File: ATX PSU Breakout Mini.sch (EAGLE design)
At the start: 39 parts, among them J1 ATX24RH, SW1 SW_PUSH_DPDT, T1 5V, T2 3V3, T3 12V, T4 GND, T5 ADJ, T6 -12V, U1 V_REG_317SINK, U2 TPS2513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

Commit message: Fixes and additions.
Thickened all traces, added resistors to the USB ports (you can use them
instead of the TPS2513)
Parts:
- added R10, R15: (no value), SparkFun-Resistors:RESISTOR0805-RES
- added R11, R16: 43K, SparkFun-Resistors:RESISTOR0805-RES
- added R12, R14, R17, R19: 51K, SparkFun-Resistors:RESISTOR0805-RES
- added R13, R18: 75K, SparkFun-Resistors:RESISTOR0805-RES
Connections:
- net 5V_STDBY: now also R16.1, R18.1
- net DM1: now also R15.1, R16.2, R17.1
- net DM2: now also R10.1, R11.2, R12.1
- net DP1: now also R15.2, R18.2, R19.1
- net DP2: now also R10.2, R13.2, R14.1
- net GND: now also R12.2, R14.2, R17.2, R19.2
- net USB_P4: now also R11.1, R13.1
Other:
- moved on the sheet: C3, R9, SJ1, U2, X1, X2

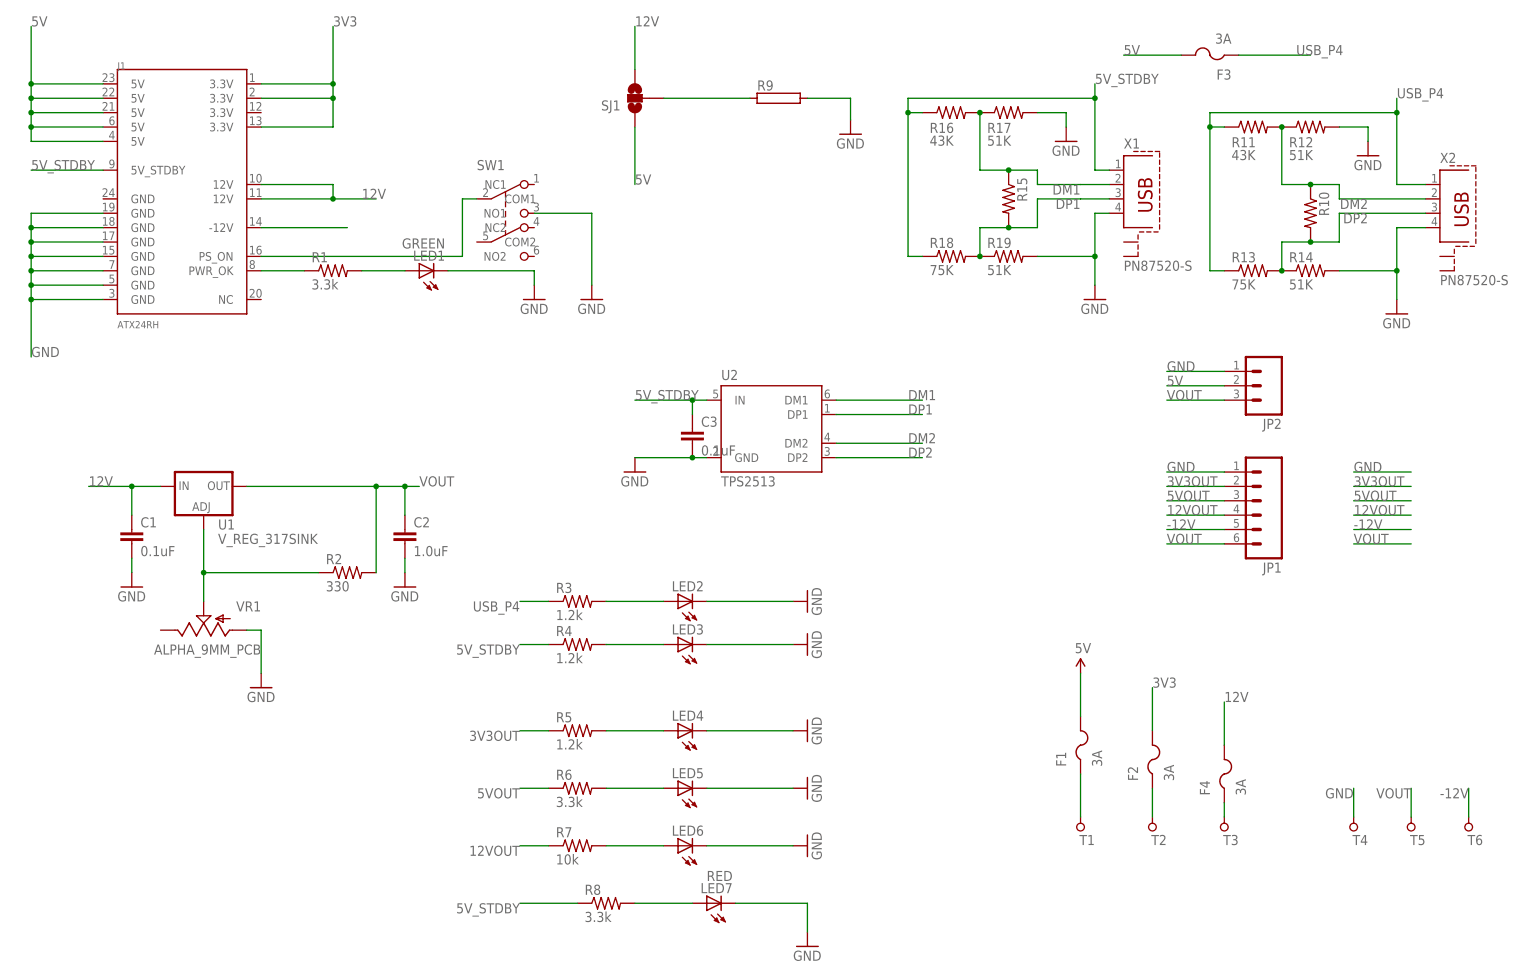
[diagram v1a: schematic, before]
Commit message: New version (v1.2)
Fixed bugs, rearranged traces and components, added pin headers, USB
resistors and prototyping area.
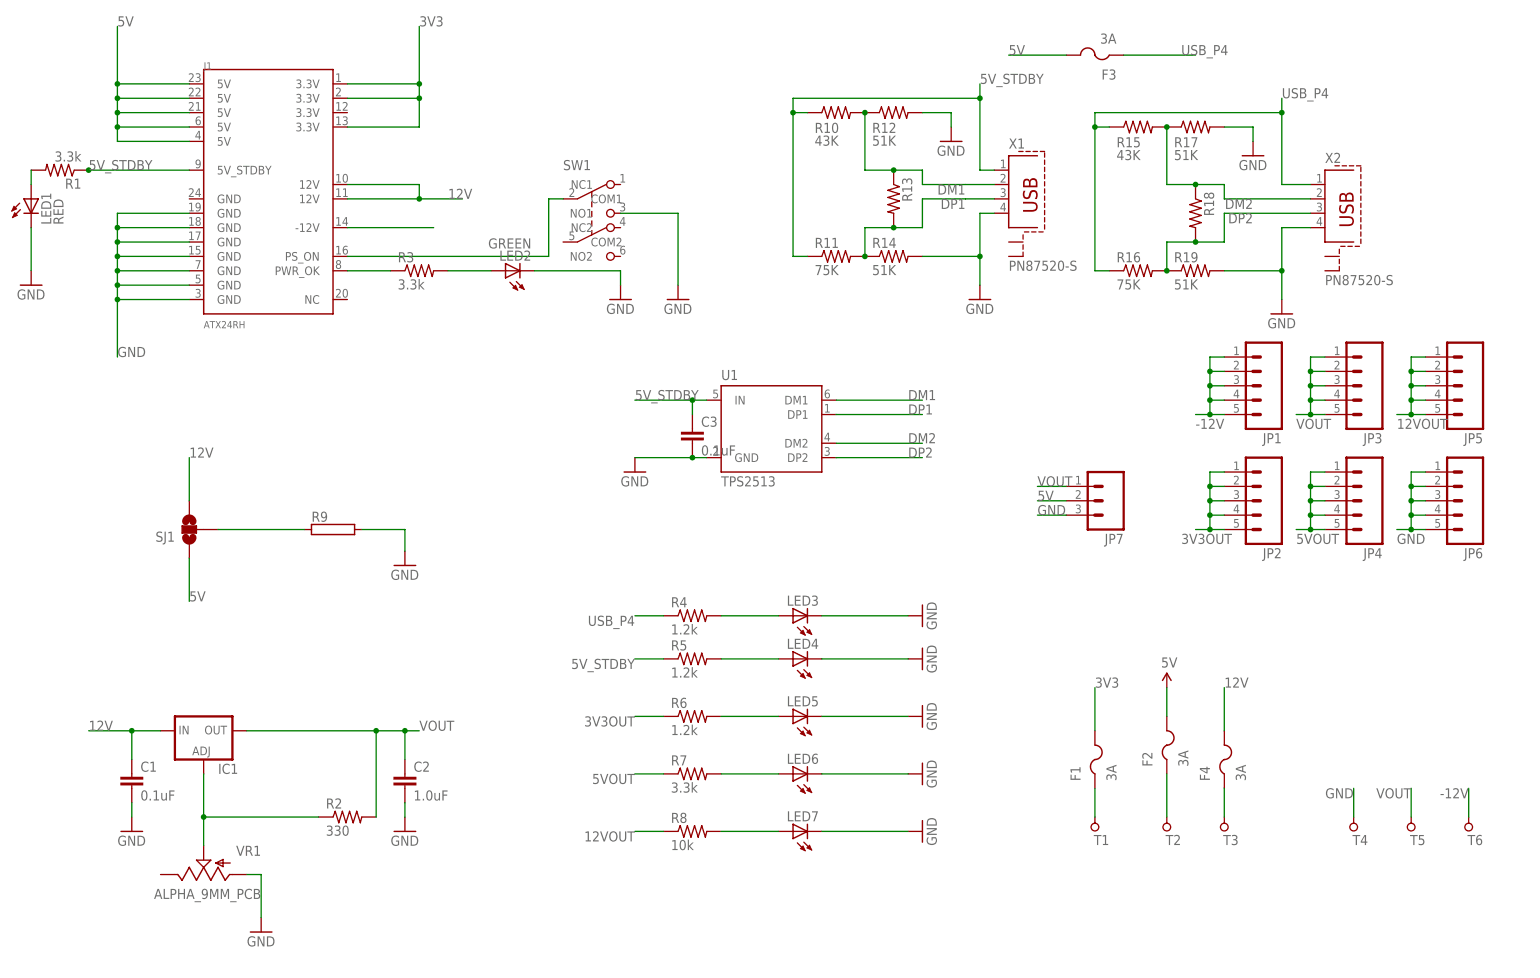
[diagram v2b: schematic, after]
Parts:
- removed U2: TPS2513, SparkFun-DigitalIC:TPS2513
- added IC1: (no value), v-reg:LM317TL
- added JP3, JP4, JP5, JP6: (no value), SparkFun-Connectors:M05PTH
- added JP7: (no value), SparkFun-Connectors:M03LOCK
- JP1: device SparkFun-Connectors:M06LOCK -> SparkFun-Connectors:M05PTH
- JP2: device SparkFun-Connectors:M03PTH -> SparkFun-Connectors:M05PTH
- LED1: value GREEN -> RED
- LED2: value (none) -> GREEN
- LED7: value RED -> (none)
- R10, R15: value (none) -> 43K
- R11, R16: value 43K -> 75K
- R13, R18: value 75K -> (none)
- R3: value 1.2k -> 3.3k
- R6: value 3.3k -> 1.2k
- R7: value 10k -> 3.3k
- R8: value 3.3k -> 10k
- T1: value 5V -> 3V3
- T2: value 3V3 -> 5V
- U1: value V_REG_317SINK -> TPS2513; device SparkFun-PowerIC:V_REG_317SINK -> SparkFun-DigitalIC:TPS2513
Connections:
- net -12V: now also JP1.1, JP1.2, JP1.3, JP1.4
- net 12V: now also IC1.IN; no longer U1.IN
- net 12VOUT: now also JP5.1, JP5.2, JP5.3, JP5.4, JP5.5, R8.1; no longer JP1.4, R7.1
- net 3V3: now also F1.2; no longer F2.2
- net 3V3OUT: now also F1.1, JP2.1, JP2.2, JP2.3, JP2.4, JP2.5, R6.1, T1.P; no longer F2.1, JP1.2, R5.1, T2.P
- net 5V: now also F2.2, JP7.2; no longer F1.2, JP2.2
- net 5VOUT: now also F2.1, JP4.1, JP4.2, JP4.3, JP4.4, JP4.5, R7.1, T2.P; no longer F1.1, JP1.3, R6.1, T1.P
- net 5V_STDBY: now also R1.1, R10.1, R11.1, R5.1, U1.IN; no longer R16.1, R18.1, R4.1, R8.1, U2.IN
- net DM1: now also R10.2, R12.1, R13.1, U1.DM1; no longer R15.1, R16.2, R17.1, U2.DM1
- net DM2: now also R15.2, R17.1, R18.1, U1.DM2; no longer R10.1, R11.2, R12.1, U2.DM2
- net DP1: now also R11.2, R13.2, R14.1, U1.DP1; no longer R15.2, R18.2, R19.1, U2.DP1
- net DP2: now also R16.2, R18.2, R19.1, U1.DP2; no longer R10.2, R13.2, R14.1, U2.DP2
- net GND: now also JP6.1, JP6.2, JP6.3, JP6.4, JP6.5, JP7.3, U1.GND; no longer JP1.1, JP2.1, U2.GND
- net N$1: now also R3.1; no longer R1.1
- net N$9: now also IC1.ADJ; no longer U1.ADJ
- net USB_P4: now also R15.1, R16.1, R4.1; no longer R11.1, R13.1, R3.1
- net VOUT: now also IC1.OUT, JP3.1, JP3.2, JP3.3, JP3.4, JP3.5, JP7.1; no longer JP1.6, JP2.3, U1.OUT
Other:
- moved on the sheet: C1, C2, F1, F2, F3, F4, J1, LED1, LED2, LED3, LED4, LED5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
